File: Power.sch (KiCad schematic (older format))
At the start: 20 parts, among them J1 Conn_02x05_Odd_Even, U3 R-78E5.0-0.5, U4 LD2981ABU33TR

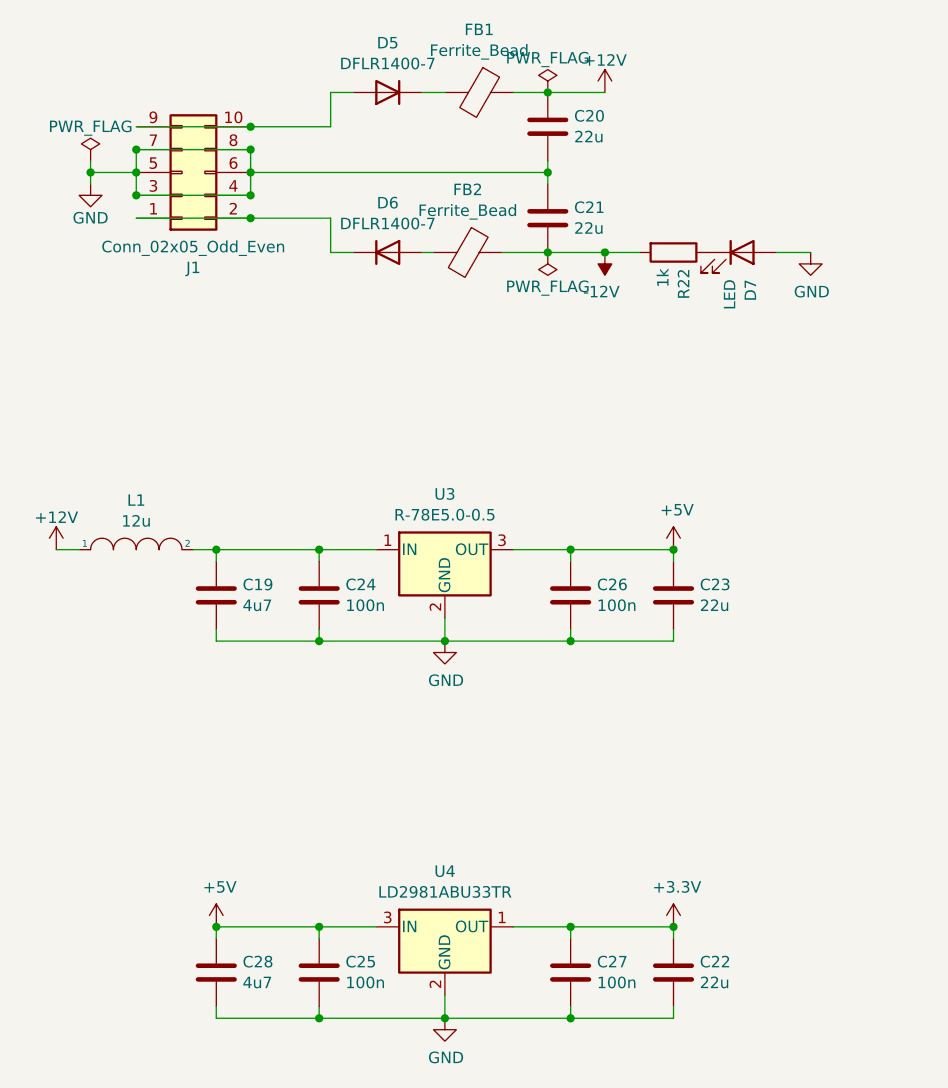
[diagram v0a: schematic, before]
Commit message: Moved audio-io to separate sheet.
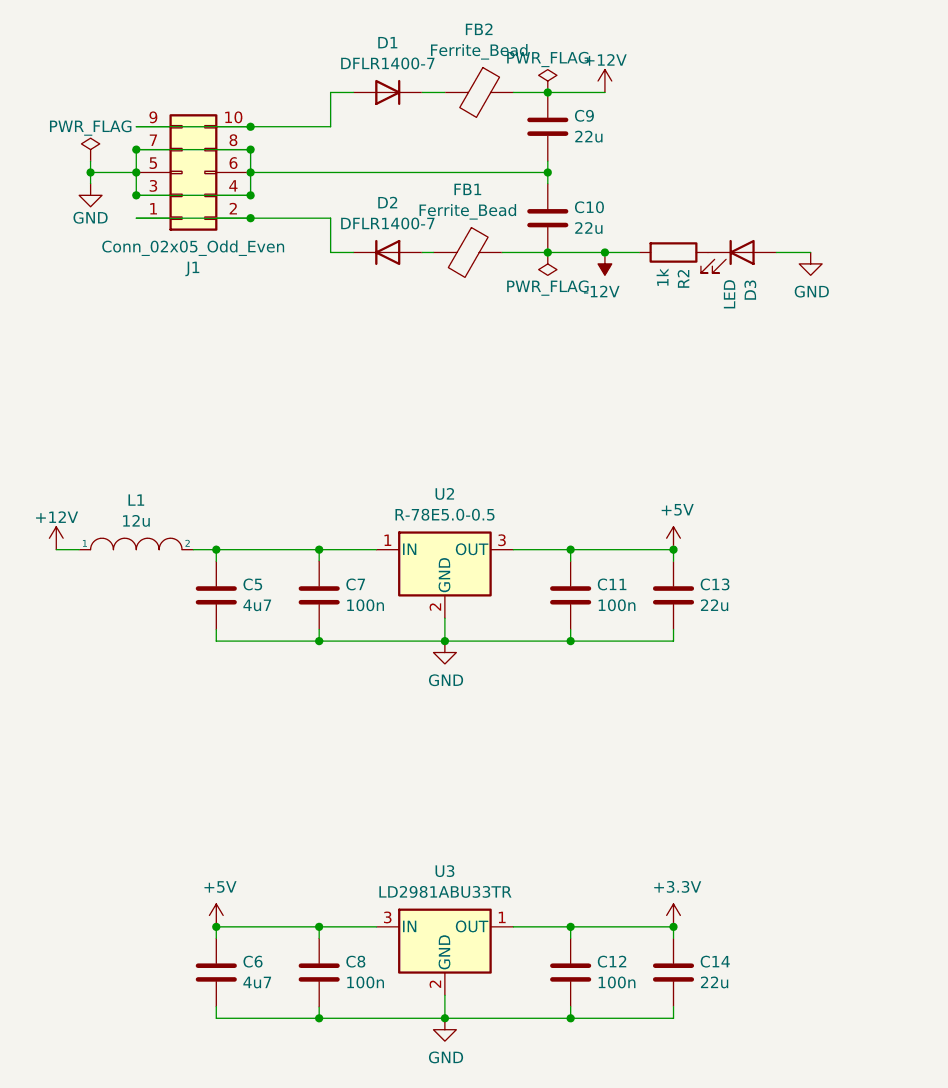
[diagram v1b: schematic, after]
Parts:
- renumbered C21 to C10, C26 to C11, C27 to C12, C23 to C13, C22 to C14, C19 to C5, C28 to C6, C24 to C7, C25 to C8, C20 to C9, D5 to D1, D6 to D2, D7 to D3, FB2 to FB1, FB1 to FB2, R22 to R2, U3 to U2, U4 to U3

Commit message: Added STM32750 mcu.
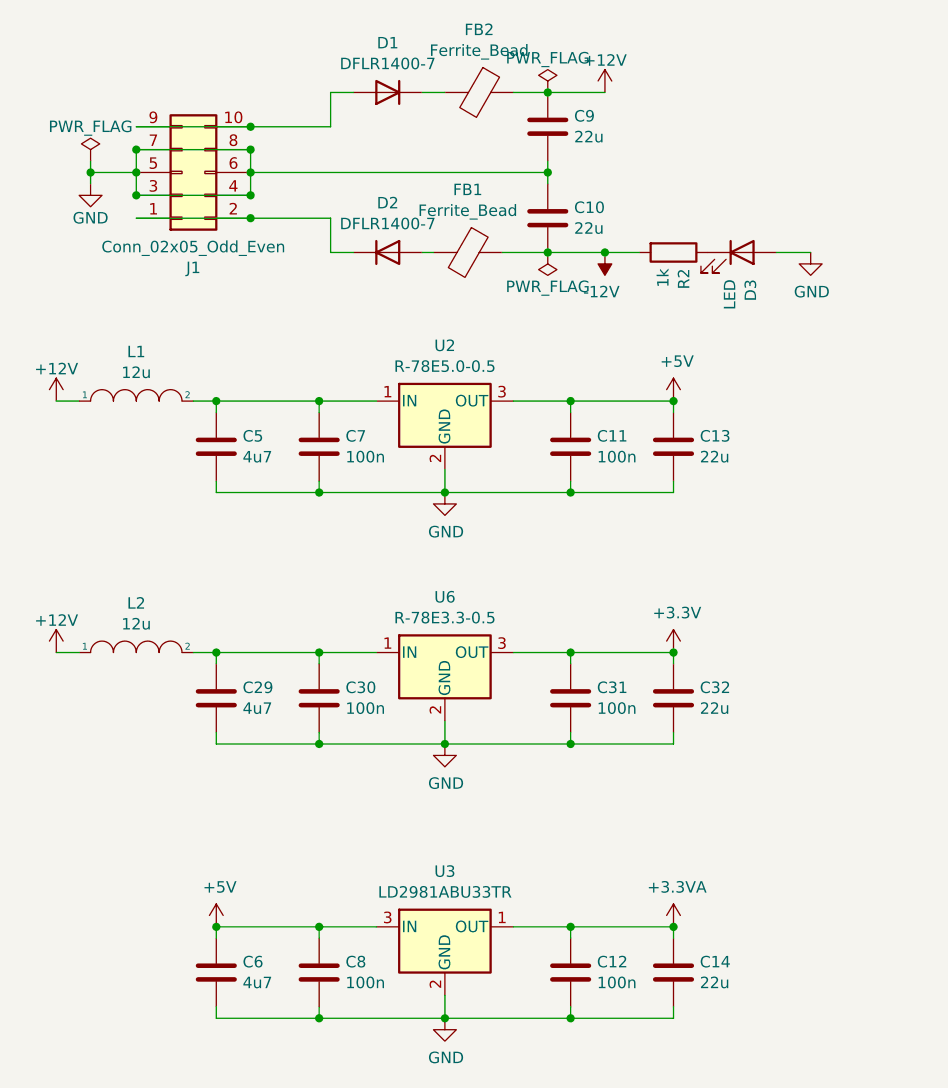
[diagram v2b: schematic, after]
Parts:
- added C29: 4u7, Capacitor_SMD:C_0805_2012Metric, symbol Device:C
- added C30, C31: 100n, Capacitor_SMD:C_0603_1608Metric, symbol Device:C
- added C32: 22u, Capacitor_SMD:C_1206_3216Metric, symbol Device:C
- added L2: 12u, Local:L_Coilcraft_LPS3010, symbol pspice:INDUCTOR
- added U6: R-78E3.3-0.5, Converter_DCDC:Converter_DCDC_RECOM_R-78E-0.5_THT, symbol Regulator_Switching:R-78E3.3-0.5
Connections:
- net +12V: now also L2.1
- net +3V3: now also C31.1, C32.1, U6.3 (OUT); no longer C12.1, C14.1, U3.1 (OUT)
- net GND: now also C29.2, C30.2, C31.2, C32.2, U6.2 (GND)
- new net: C29.1, C30.1, L2.2, U6.1 (IN)
- new net +3.3VA: C12.1, C14.1, U3.1 (OUT)
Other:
- moved on the sheet: C11, C13, C5, C7, L1, U2

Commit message: Chanced regulators and oscillator work.
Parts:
- removed C11, C7: 100n, Capacitor_SMD:C_0603_1608Metric, symbol Device:C
- removed C13: 22u, Capacitor_SMD:C_1206_3216Metric, symbol Device:C
- removed C5: 4u7, Capacitor_SMD:C_0805_2012Metric, symbol Device:C
- removed L1: 12u, Local:L_Coilcraft_LPS3010, symbol pspice:INDUCTOR
- removed U2: R-78E5.0-0.5, Converter_DCDC:Converter_DCDC_RECOM_R-78E-0.5_THT, symbol Regulator_Switching:R-78E5.0-0.5
- removed U3: LD2981ABU33TR, Package_TO_SOT_SMD:SOT-89-3, symbol Local:LD2981ABU33TR
- added U4: LD2981ABU50TR, Package_TO_SOT_SMD:SOT-89-3, symbol LD2981:LD2981ABU50TR
- C22: renamed from C30; footprint Capacitor_SMD:C_0603_1608Metric -> Capacitor_SMD:C_0402_1005Metric
- C23: renamed from C8; footprint Capacitor_SMD:C_0603_1608Metric -> Capacitor_SMD:C_0402_1005Metric
- C26: renamed from C31; footprint Capacitor_SMD:C_0603_1608Metric -> Capacitor_SMD:C_0402_1005Metric
- C27: renamed from C12; footprint Capacitor_SMD:C_0603_1608Metric -> Capacitor_SMD:C_0402_1005Metric
- renumbered C29 to C20, C6 to C21, C9 to C24, C10 to C25, C32 to C28, C14 to C29, L2 to L1, R2 to R5, U6 to U3
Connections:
- net +3.3VA is gone; now on net +5V: C27.1, C29.1
- net +12V: now also C21.1, C23.1, U4.3 (IN)
- net +5V: now also U4.1 (OUT); no longer C21.1, C23.1
- net GND: now also U4.2 (GND)
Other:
- moved on the sheet: C20, C21, C22, C23, C26, C27, C28, C29, L1, U3

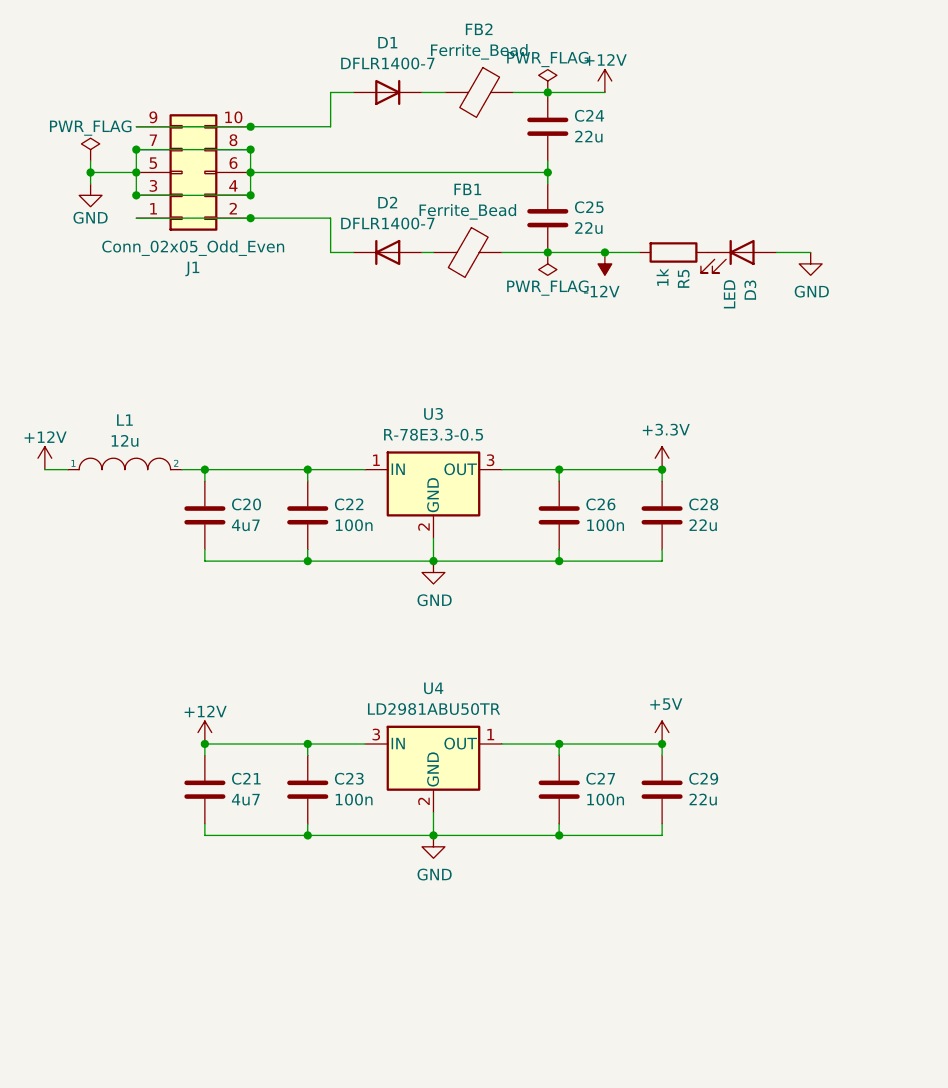
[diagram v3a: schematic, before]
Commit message: Added UI components.
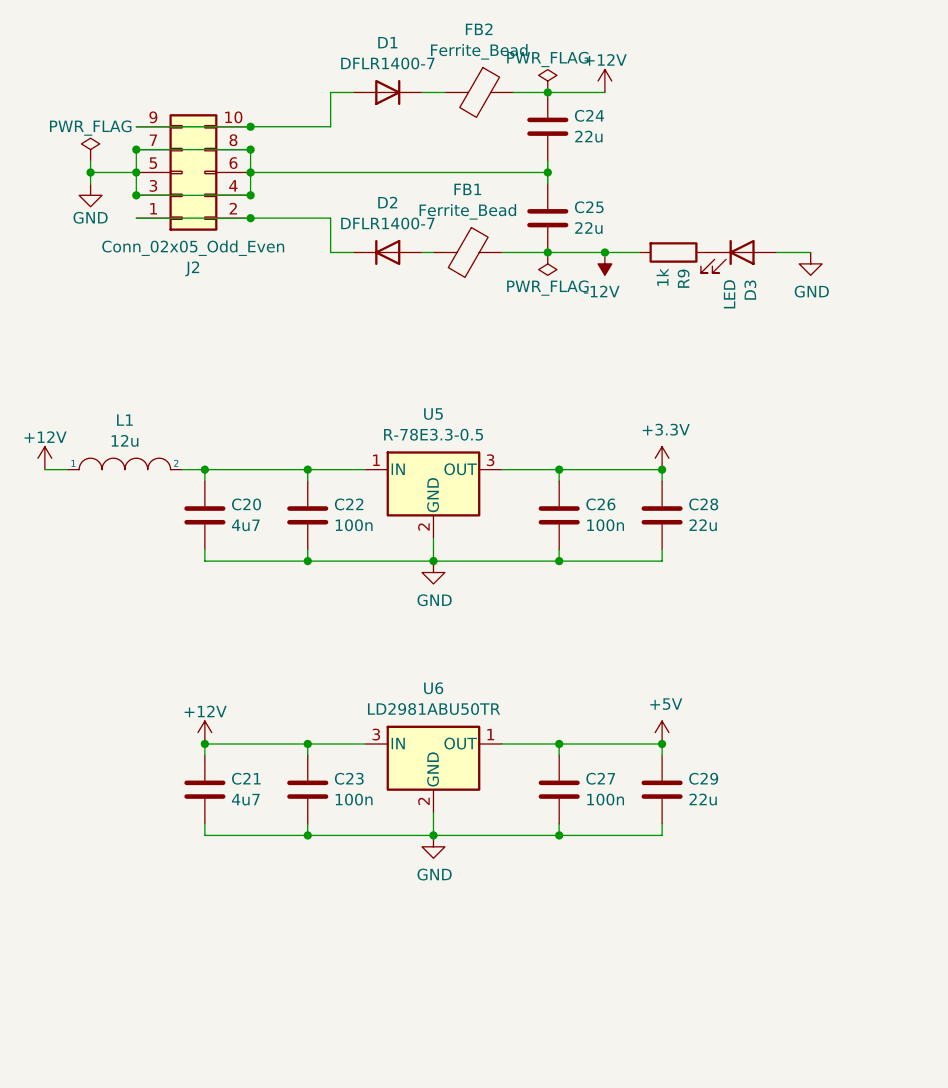
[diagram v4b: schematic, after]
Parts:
- renumbered J1 to J2, R5 to R9, U3 to U5, U4 to U6
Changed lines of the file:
@@
 $Descr A4 11693 8268
 encoding utf-8
-Sheet 2 3
+Sheet 2 6
 Title ""
 Date ""
@@
 AR Path="/61C9E219" Ref="R?"  Part="1"
 AR Path="/61C5176D/61C9E219" Ref="R?"  Part="1"
-AR Path="/61C80AC7/61C9E219" Ref="R5"  Part="1"
-F 0 "R5" H 5470 2446 50  0000 L CNN
+AR Path="/61C80AC7/61C9E219" Ref="R9"  Part="1"
+F 0 "R9" H 5470 2446 50  0000 L CNN
 F 1 "1k" H 5470 2355 50  0000 L CNN
 F 2 "Resistor_SMD:R_0603_1608Metric" V 5330 2400 50  0001 C CNN
@@
 AR Path="/61C9E21F" Ref="#PWR?"  Part="1"
 AR Path="/61C5176D/61C9E21F" Ref="#PWR?"  Part="1"
-AR Path="/61C80AC7/61C9E21F" Ref="#PWR032"  Part="1"
-F 0 "#PWR032" H 6000 2150 50  0001 C CNN
+AR Path="/61C80AC7/61C9E21F" Ref="#PWR040"  Part="1"
+F 0 "#PWR040" H 6000 2150 50  0001 C CNN
 F 1 "GND" H 6005 2227 50  0000 C CNN
 F 2 "" H 6000 2400 50  0001 C CNN
@@
 AR Path="/61C9E235" Ref="J?"  Part="1"
 AR Path="/61C5176D/61C9E235" Ref="J?"  Part="1"
-AR Path="/61C80AC7/61C9E235" Ref="J1"  Part="1"
-F 0 "J1" H 3300 2467 50  0000 C CNN
+AR Path="/61C80AC7/61C9E235" Ref="J2"  Part="1"
+F 0 "J2" H 3300 2467 50  0000 C CNN
 F 1 "Conn_02x05_Odd_Even" H 3300 2376 50  0000 C CNN
 F 2 "Connector_PinHeader_2.54mm:PinHeader_2x05_P2.54mm_Vertical" H 3250 2050 50  0001 C CNN
@@
 AR Path="/61C9E253" Ref="#PWR?"  Part="1"
 AR Path="/61C5176D/61C9E253" Ref="#PWR?"  Part="1"
-AR Path="/61C80AC7/61C9E253" Ref="#PWR024"  Part="1"
-F 0 "#PWR024" H 2850 1850 50  0001 C CNN
+AR Path="/61C80AC7/61C9E253" Ref="#PWR032"  Part="1"
+F 0 "#PWR032" H 2850 1850 50  0001 C CNN
 F 1 "GND" H 2850 1950 50  0000 C CNN
 F 2 "" H 2850 2100 50  0001 C CNN
@@
 AR Path="/61C9E2C9" Ref="#PWR?"  Part="1"
 AR Path="/61C5176D/61C9E2C9" Ref="#PWR?"  Part="1"
-AR Path="/61C80AC7/61C9E2C9" Ref="#PWR027"  Part="1"
-F 0 "#PWR027" H 4350 4700 50  0001 C CNN
+AR Path="/61C80AC7/61C9E2C9" Ref="#PWR035"  Part="1"
+F 0 "#PWR035" H 4350 4700 50  0001 C CNN
 F 1 "GND" H 4355 4777 50  0000 C CNN
 F 2 "" H 4350 4950 50  0001 C CNN
@@
 AR Path="/61C9E2D7" Ref="#PWR?"  Part="1"
 AR Path="/61C5176D/61C9E2D7" Ref="#PWR?"  Part="1"
-AR Path="/61C80AC7/61C9E2D7" Ref="#PWR028"  Part="1"
-F 0 "#PWR028" H 5100 1550 50  0001 C CNN
+AR Path="/61C80AC7/61C9E2D7" Ref="#PWR036"  Part="1"
+F 0 "#PWR036" H 5100 1550 50  0001 C CNN
 F 1 "+12V" H 5100 1840 50  0000 C CNN
 F 2 "" H 5100 1700 50  0001 C CNN
@@
 	4300 1700 4400 1700
 $Comp
-L power:-12V #PWR029
+L power:-12V #PWR037
 U 1 1 61A6FD5E
 P 5100 2400
-F 0 "#PWR029" H 5100 2500 50  0001 C CNN
+F 0 "#PWR037" H 5100 2500 50  0001 C CNN
 F 1 "-12V" H 5115 2573 50  0000 C CNN
 F 2 "" H 5100 2400 50  0001 C CNN
@@
 $EndComp
 $Comp
-L power:+3.3V #PWR030
+L power:+3.3V #PWR038
 U 1 1 61B17B4F
 P 5350 3350
-F 0 "#PWR030" H 5350 3200 50  0001 C CNN
+F 0 "#PWR038" H 5350 3200 50  0001 C CNN
 F 1 "+3.3V" H 5365 3523 50  0000 C CNN
 F 2 "" H 5350 3350 50  0001 C CNN
@@
 AR Path="/61D89AAC" Ref="#PWR?"  Part="1"
 AR Path="/61C5176D/61D89AAC" Ref="#PWR?"  Part="1"
-AR Path="/61C80AC7/61D89AAC" Ref="#PWR026"  Part="1"
-F 0 "#PWR026" H 4350 3500 50  0001 C CNN
+AR Path="/61C80AC7/61D89AAC" Ref="#PWR034"  Part="1"
+F 0 "#PWR034" H 4350 3500 50  0001 C CNN
 F 1 "GND" H 4355 3577 50  0000 C CNN
 F 2 "" H 4350 3750 50  0001 C CNN
@@
 AR Path="/61D89ACC" Ref="#PWR?"  Part="1"
 AR Path="/61C5176D/61D89ACC" Ref="#PWR?"  Part="1"
-AR Path="/61C80AC7/61D89ACC" Ref="#PWR023"  Part="1"
-F 0 "#PWR023" H 2650 3200 50  0001 C CNN
+AR Path="/61C80AC7/61D89ACC" Ref="#PWR031"  Part="1"
+F 0 "#PWR031" H 2650 3200 50  0001 C CNN
 F 1 "+12V" H 2650 3490 50  0000 C CNN
 F 2 "" H 2650 3350 50  0001 C CNN
@@
 $EndComp
 $Comp
-L Regulator_Switching:R-78E3.3-0.5 U3
+L Regulator_Switching:R-78E3.3-0.5 U5
 U 1 1 61D8F6E2
 P 4350 3350
-F 0 "U3" H 4350 3592 50  0000 C CNN
+F 0 "U5" H 4350 3592 50  0000 C CNN
 F 1 "R-78E3.3-0.5" H 4350 3501 50  0000 C CNN
 F 2 "Converter_DCDC:Converter_DCDC_RECOM_R-78E-0.5_THT" H 4400 3100 50  0001 L CIN
@@
 Connection ~ 5350 3350
 $Comp
-L power:+5V #PWR031
+L power:+5V #PWR039
 U 1 1 61AB9C33
 P 5350 4550
-F 0 "#PWR031" H 5350 4400 50  0001 C CNN
+F 0 "#PWR039" H 5350 4400 50  0001 C CNN
 F 1 "+5V" H 5365 4723 50  0000 C CNN
 F 2 "" H 5350 4550 50  0001 C CNN
@@
 AR Path="/61ACBF55" Ref="#PWR?"  Part="1"
 AR Path="/61C5176D/61ACBF55" Ref="#PWR?"  Part="1"
-AR Path="/61C80AC7/61ACBF55" Ref="#PWR025"  Part="1"
-F 0 "#PWR025" H 3350 4400 50  0001 C CNN
+AR Path="/61C80AC7/61ACBF55" Ref="#PWR033"  Part="1"
+F 0 "#PWR033" H 3350 4400 50  0001 C CNN
 F 1 "+12V" H 3350 4690 50  0000 C CNN
 F 2 "" H 3350 4550 50  0001 C CNN
@@
 Connection ~ 3350 4550
 $Comp
-L LD2981:LD2981ABU50TR U4
+L LD2981:LD2981ABU50TR U6
 U 1 1 61AD1D02
 P 4350 4550
-F 0 "U4" H 4350 4792 50  0000 C CNN
+F 0 "U6" H 4350 4792 50  0000 C CNN
 F 1 "LD2981ABU50TR" H 4350 4701 50  0000 C CNN
 F 2 "Package_TO_SOT_SMD:SOT-89-3" H 4350 4750 50  0001 C CIN
